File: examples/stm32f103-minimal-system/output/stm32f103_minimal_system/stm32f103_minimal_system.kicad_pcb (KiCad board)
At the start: 129 x 176.5 mm, 18 parts, among them J1 USB-C16PIN, J2 SWD-4P, SW1 SW-TH_6x6, U1 STM32F103C8T6, U2 AMS1117-3.3, Y1 8MHz

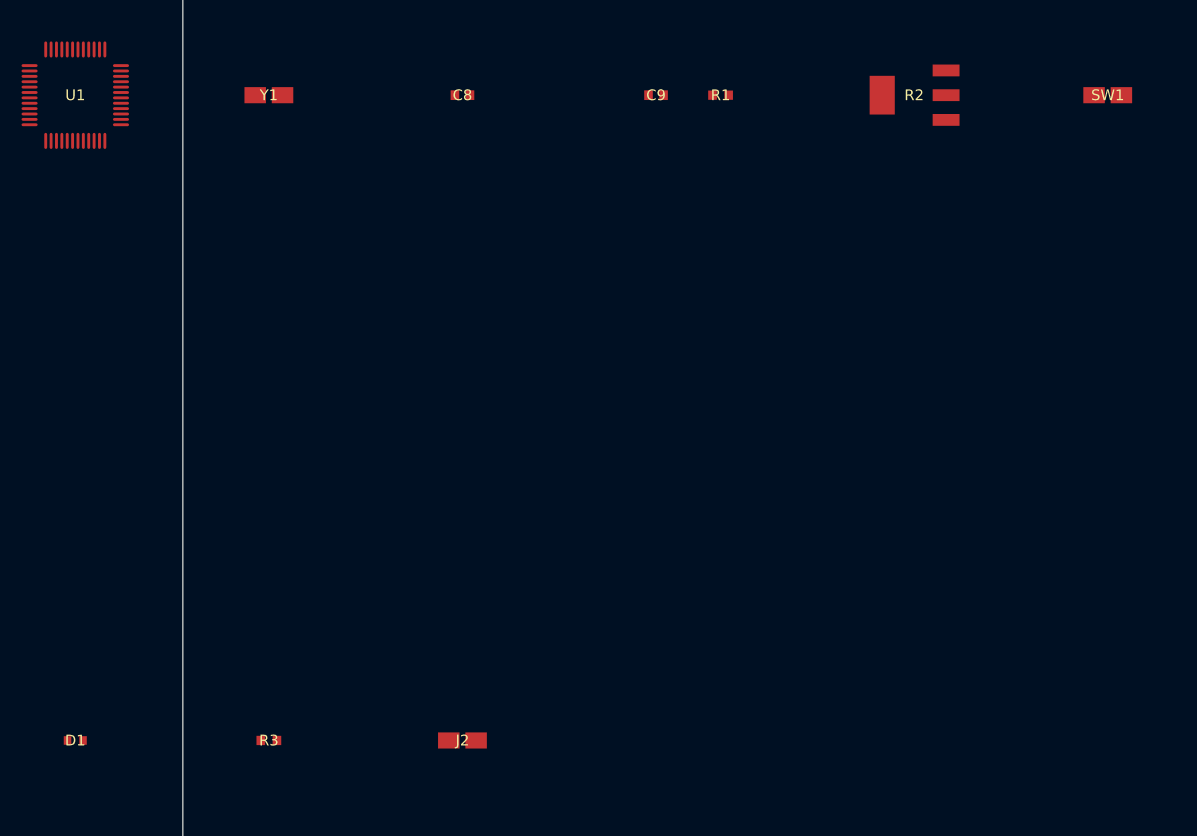
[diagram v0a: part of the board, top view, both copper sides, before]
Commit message: chore(example): update STM32F103 with pcb_layout regions and latest build output 更新示例：PCB 区域布局 + 最新构建输出
- Add pcb_layout.regions with 7 functional areas (power, regulation, decoupling, mcu, clock, reset_boot, led_io)
- Refresh schematics, ERC, reports, and operation logs

Co-Authored-By: Claude Opus 4.7 <noreply@anthropic.com>
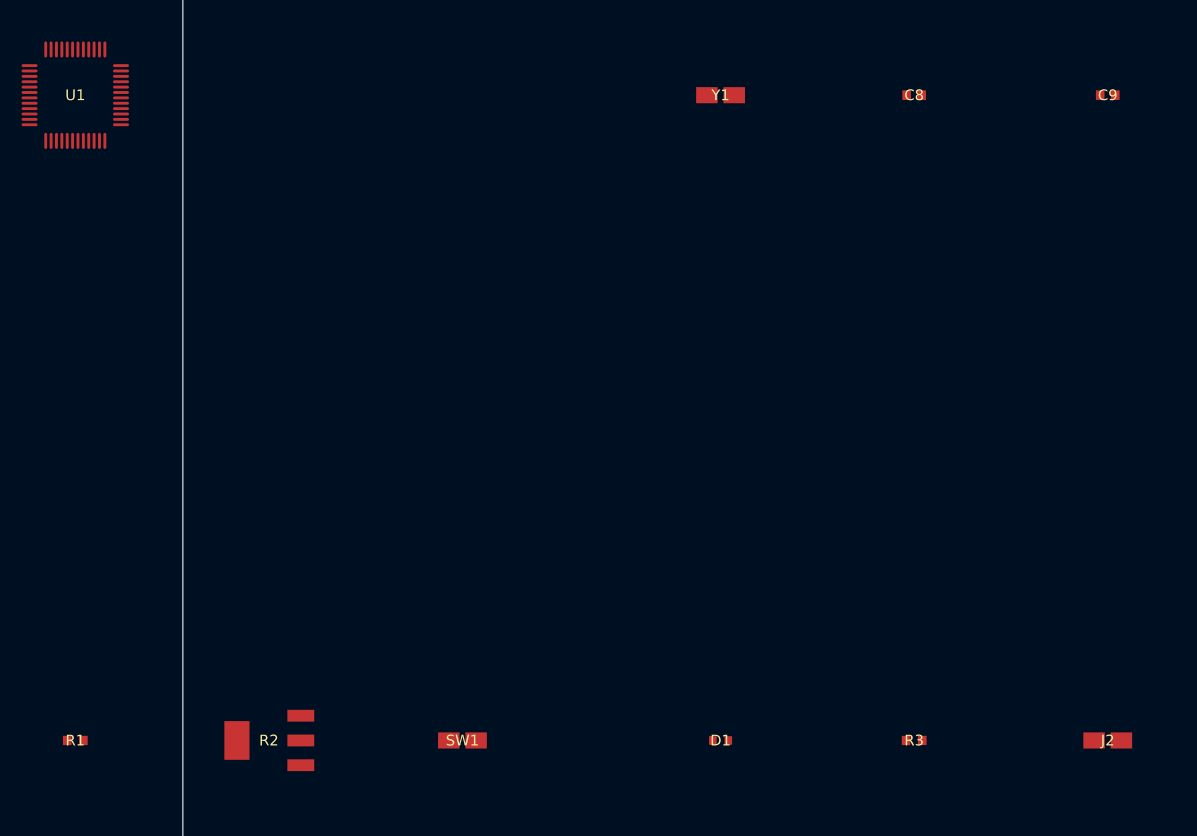
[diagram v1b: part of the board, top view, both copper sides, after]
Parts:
- moved R1 84.9 mm to (10.0, 160.0)
- moved R2 84.9 mm to (28.0, 160.0)
- moved SW1 84.9 mm to (46.0, 160.0)
- moved D1 60.0 mm to (70.0, 160.0)
- moved J2 60.0 mm to (106.0, 160.0)
- moved R3 60.0 mm to (88.0, 160.0)
- moved C8 42.0 mm to (88.0, 100.0)
- moved C9 42.0 mm to (106.0, 100.0)
- moved Y1 42.0 mm to (70.0, 100.0)
